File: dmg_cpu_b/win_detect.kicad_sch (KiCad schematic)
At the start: 127 parts

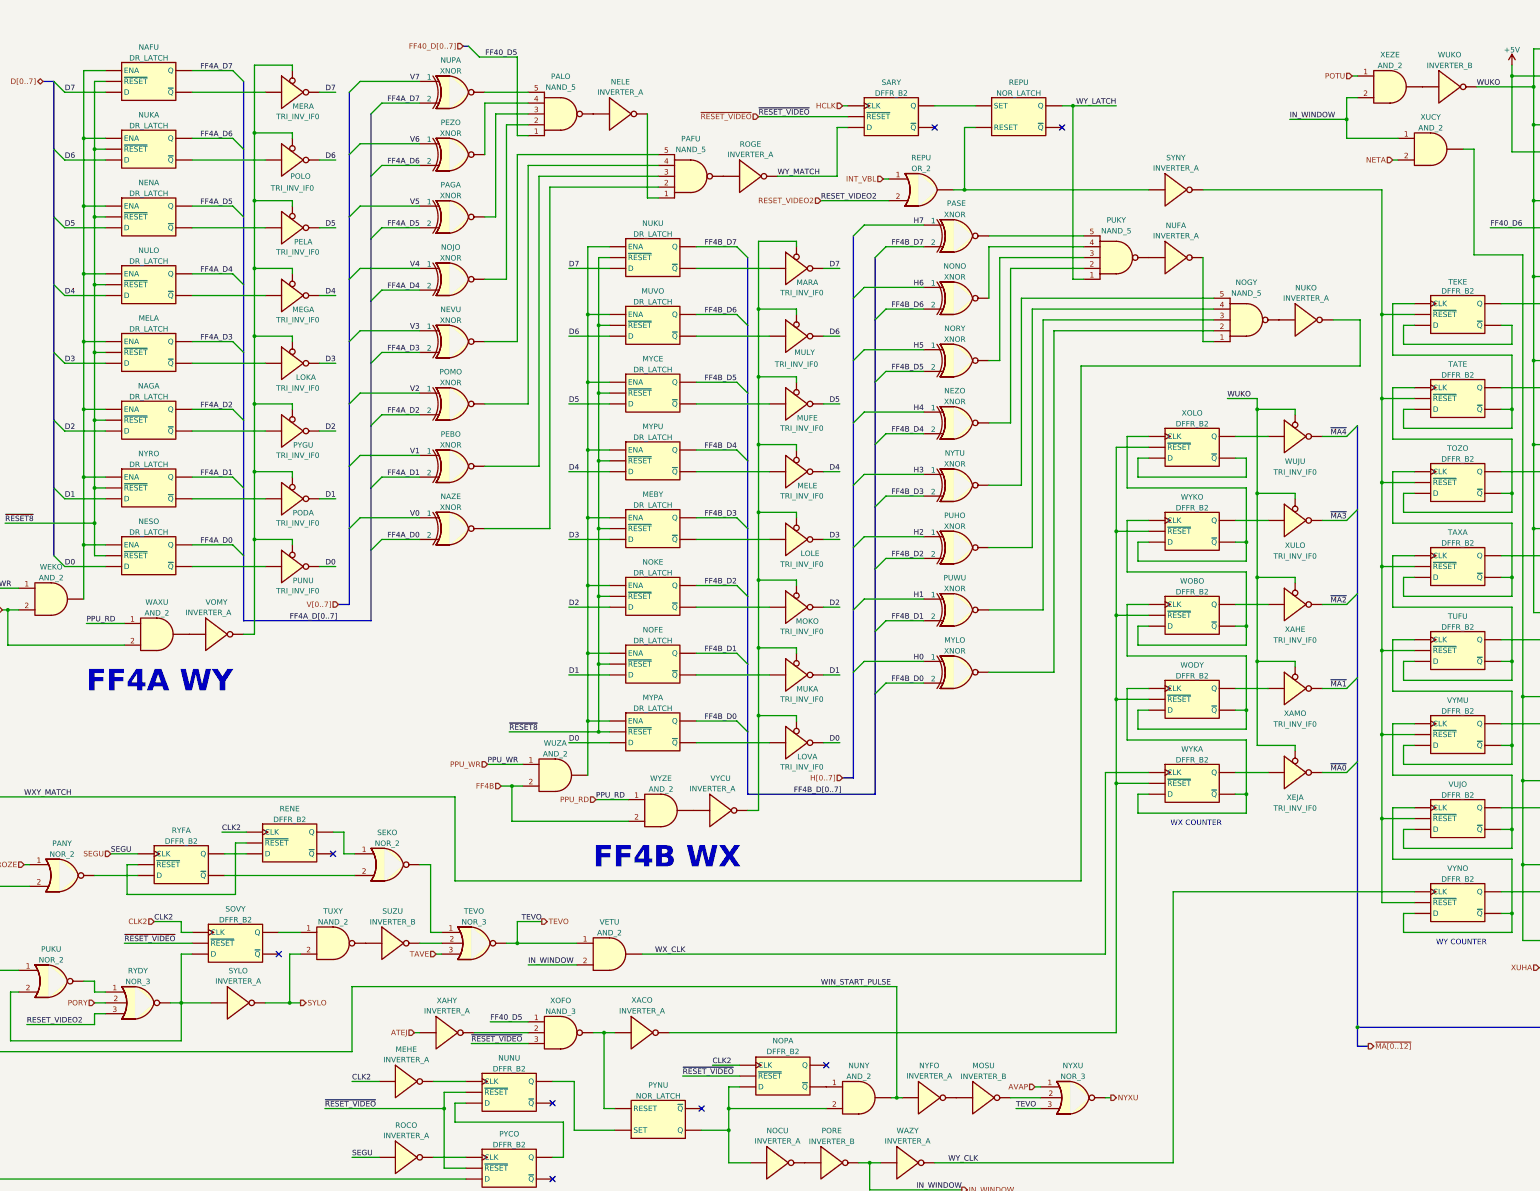
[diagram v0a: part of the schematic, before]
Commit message: Some mistakes found in APU sheets, notes added for clarity. Edit in PPU sheets following review.
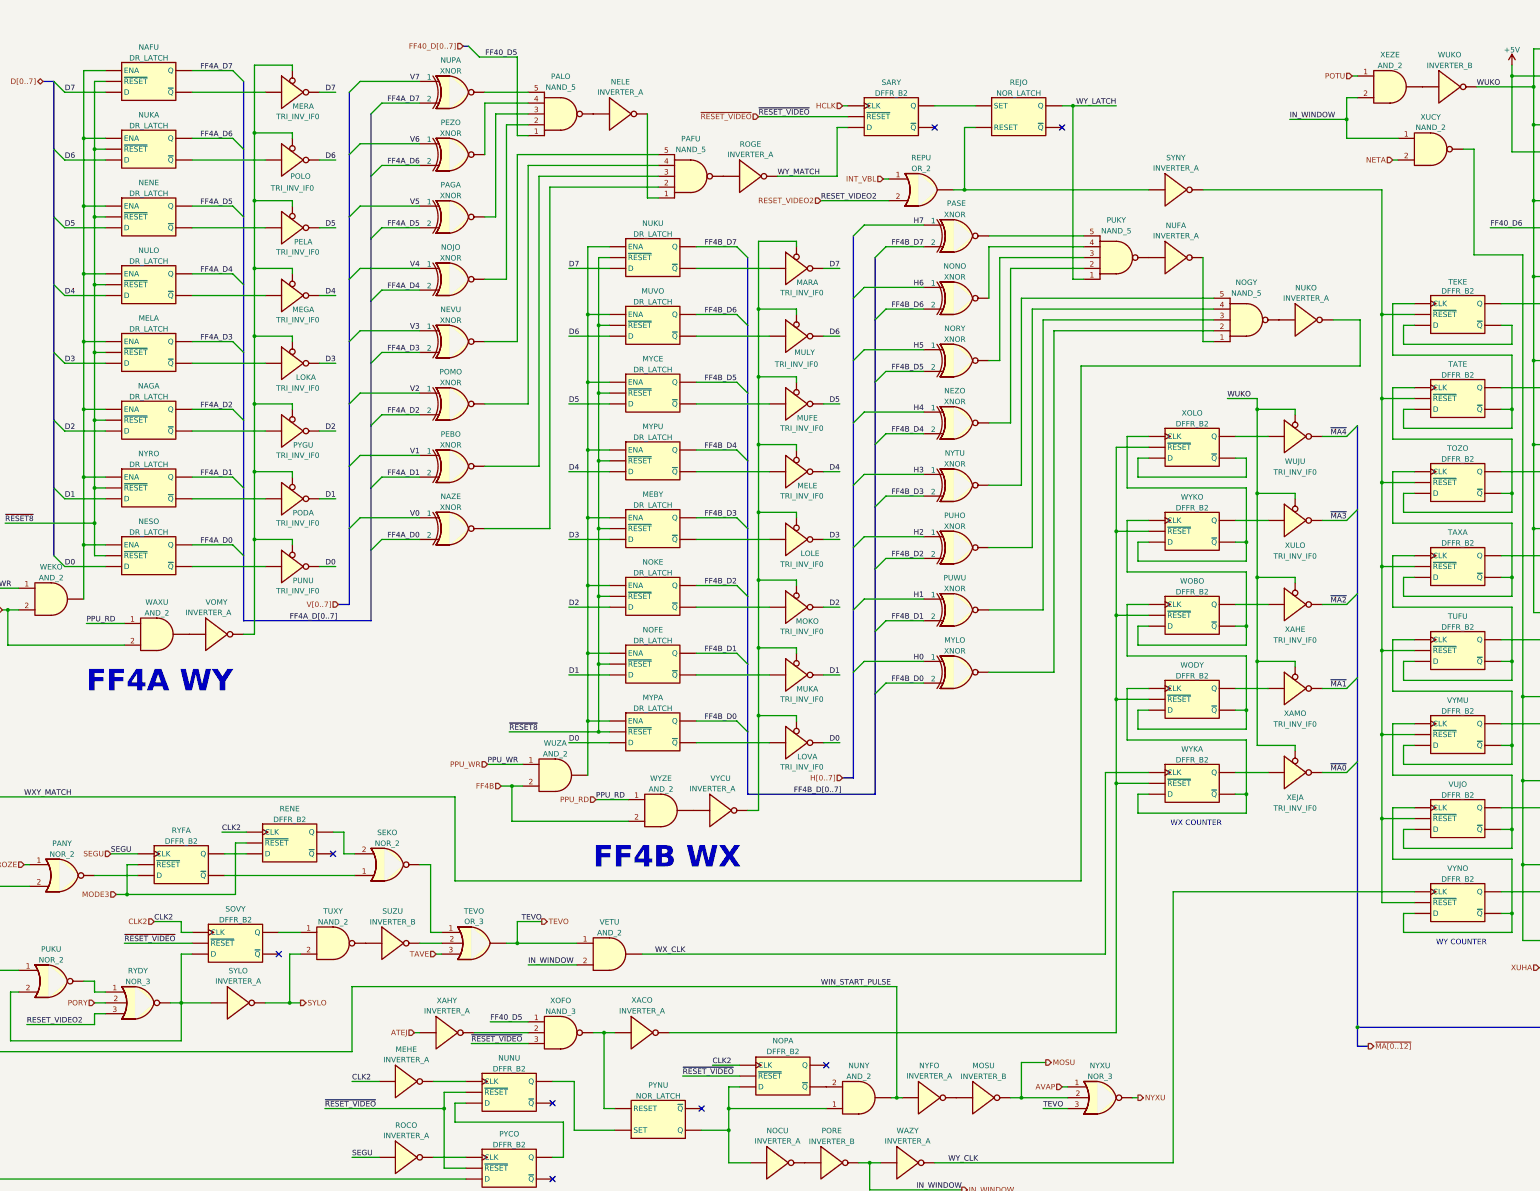
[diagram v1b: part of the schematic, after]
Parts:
- TEVO: value NOR_3 -> OR_3; symbol DMG_CPU_Cells:NOR_3 -> DMG_CPU_Cells:OR_3
- XUCY: value AND_2 -> NAND_2; symbol DMG_CPU_Cells:AND_2 -> DMG_CPU_Cells:NAND_2
- renumbered NENA to NENE, REPU to REJO
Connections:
- net at NOCU.1, NOPA.3 (D), PYNU.3 (Q): now also NUNY.1; no longer NUNY.2
- net at NOPA.5 (~{Q}): now also NUNY.2; no longer NUNY.1
- net MODE3: now reaches RENE.2 (~{RESET}), RENE.4 (~{RESET}), RYFA.2 (~{RESET}), RYFA.4 (~{RESET})
- net at RYFA.5 (~{Q}): now also SEKO.1; no longer SEKO.2
- net at RENE.6 (Q): now also SEKO.2; no longer SEKO.1
- net MOSU: now reaches MOSU.2, NYXU.2
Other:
- moved on the sheet: NYXU
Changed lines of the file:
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@@
   (junction (at 346.075 175.895) (diameter 0) (color 0 0 0 0)
   )
+  (junction (at 261.62 260.985) (diameter 0) (color 0 0 0 0)
+  )
   (junction (at 90.17 238.76) (diameter 0) (color 0 0 0 0)
   )
@@
   (junction (at 44.45 54.61) (diameter 0) (color 0 0 0 0)
   )
+  (junction (at 52.07 213.36) (diameter 0) (color 0 0 0 0)
+  )
   (junction (at 41.91 52.07) (diameter 0) (color 0 0 0 0)
   )
@@
     (stroke (width 0) (type default) (color 0 0 0 0))
   )
+  (wire (pts (xy 261.62 260.985) (xy 259.08 260.985))
+    (stroke (width 0) (type default) (color 0 0 0 0))
+  )
   (wire (pts (xy 104.775 274.955) (xy 111.125 274.955))
     (stroke (width 0) (type default) (color 0 0 0 0))
@@
     (stroke (width 0) (type default) (color 0 0 0 0))
   )
-  (wire (pts (xy 281.305 260.985) (xy 282.575 260.985))
+  (wire (pts (xy 287.655 260.985) (xy 288.925 260.985))
     (stroke (width 0) (type default) (color 0 0 0 0))
   )
@@
     (stroke (width 0) (type default) (color 0 0 0 0))
   )
+  (wire (pts (xy 261.62 252.73) (xy 267.335 252.73))
+    (stroke (width 0) (type default) (color 0 0 0 0))
+  )
   (wire (pts (xy 41.91 20.32) (xy 46.99 20.32))
     (stroke (width 0) (type default) (color 0 0 0 0))
@@
     (stroke (width 0) (type default) (color 0 0 0 0))
   )
+  (wire (pts (xy 49.53 213.36) (xy 52.07 213.36))
+    (stroke (width 0) (type default) (color 0 0 0 0))
+  )
   (bus (pts (xy 219.71 186.055) (xy 222.25 186.055))
     (stroke (width 0) (type default) (color 0 0 0 0))
@@
     (stroke (width 0) (type default) (color 0 0 0 0))
   )
-  (wire (pts (xy 266.065 263.525) (xy 260.35 263.525))
+  (wire (pts (xy 272.415 263.525) (xy 266.7 263.525))
     (stroke (width 0) (type default) (color 0 0 0 0))
   )
@@
     (stroke (width 0) (type default) (color 0 0 0 0))
   )
-  (wire (pts (xy 266.065 260.985) (xy 259.08 260.985))
+  (wire (pts (xy 272.415 260.985) (xy 261.62 260.985))
     (stroke (width 0) (type default) (color 0 0 0 0))
   )
@@
     (stroke (width 0) (type default) (color 0 0 0 0))
   )
+  (wire (pts (xy 261.62 260.985) (xy 261.62 252.73))
+    (stroke (width 0) (type default) (color 0 0 0 0))
+  )
   (wire (pts (xy 254 102.87) (xy 259.08 102.87))
     (stroke (width 0) (type default) (color 0 0 0 0))
@@
     (stroke (width 0) (type default) (color 0 0 0 0))
   )
-  (wire (pts (xy 264.795 258.445) (xy 266.065 258.445))
+  (wire (pts (xy 271.145 258.445) (xy 272.415 258.445))
     (stroke (width 0) (type default) (color 0 0 0 0))
   )
@@
     (effects (font (size 1.27 1.27)) (justify right bottom))
   )
-  (label "TEVO" (at 260.35 263.525 0)
+  (label "TEVO" (at 266.7 263.525 0)
     (effects (font (size 1.27 1.27)) (justify left bottom))
   )
@@
     (effects (font (size 1.27 1.27)) (justify right))
   )
-  (hierarchical_label "NYXU" (shape output) (at 282.575 260.985 0)
+  (hierarchical_label "NYXU" (shape output) (at 288.925 260.985 0)
     (effects (font (size 1.27 1.27)) (justify left))
   )
@@
     (effects (font (size 1.27 1.27)) (justify right))
   )
+  (hierarchical_label "MOSU" (shape output) (at 267.335 252.73 0)
+    (effects (font (size 1.27 1.27)) (justify left))
+  )
   (hierarchical_label "H[0..7]" (shape input) (at 219.71 186.055 180)
     (effects (font (size 1.27 1.27)) (justify right))
@@
     (effects (font (size 1.27 1.27)) (justify right))
   )
+  (hierarchical_label "MODE3" (shape input) (at 49.53 213.36 180)
+    (effects (font (size 1.27 1.27)) (justify right))
+  )
   (hierarchical_label "~{MA[0..12]}" (shape output) (at 342.9 248.92 0)
     (effects (font (size 1.27 1.27)) (justify left))
@@
     (effects (font (size 1.27 1.27)) (justify right))
   )
-  (hierarchical_label "AVAP" (shape input) (at 264.795 258.445 180)
+  (hierarchical_label "AVAP" (shape input) (at 271.145 258.445 180)
     (effects (font (size 1.27 1.27)) (justify right))
   )
@@
   (symbol (lib_id "DMG_CPU_Cells:NOR_LATCH") (at 260.985 31.115 0) (unit 1)
     (in_bom yes) (on_board yes) (fields_autoplaced)
-    (property "Reference" "REPU" (id 0) (at 260.985 23.0972 0))
+    (property "Reference" "REJO" (id 0) (at 260.985 23.0972 0))
     (property "Value" "NOR_LATCH" (id 1) (at 260.985 25.6341 0))
     (property "Footprint" "" (id 2) (at 260.985 31.115 0)
@@
     (pin "6")
   )
-  (symbol (lib_id "DMG_CPU_Cells:NOR_2") (at 113.03 206.375 0) (unit 1)
+  (symbol (lib_id "DMG_CPU_Cells:NOR_2") (at 113.03 206.375 0) (mirror x) (unit 1)
     (in_bom yes) (on_board yes) (fields_autoplaced)
     (property "Reference" "SEKO" (id 0) (at 113.0298 198.8652 0))
@@
       (effects (font (size 1.27 1.27)) hide)
     )
-    (property "Datasheet" "http://iceboy.a-singer.de/doc/dmg_cells.html#nor2" (id 3) (at 113.03 213.995 0)
+    (property "Datasheet" "http://iceboy.a-singer.de/doc/dmg_cells.html#nor2" (id 3) (at 113.03 198.755 0)
       (effects (font (size 1.27 1.27)) hide)
     )
@@
     (pin "1")
   )
-  (symbol (lib_id "DMG_CPU_Cells:AND_2") (at 223.52 260.985 0) (unit 1)
+  (symbol (lib_id "DMG_CPU_Cells:AND_2") (at 223.52 260.985 0) (mirror x) (unit 1)
     (in_bom yes) (on_board yes) (fields_autoplaced)
     (property "Reference" "NUNY" (id 0) (at 223.52 253.4752 0))
@@
       (effects (font (size 1.27 1.27)) hide)
     )
-    (property "Datasheet" "http://iceboy.a-singer.de/doc/dmg_cells.html#and2" (id 3) (at 223.52 268.605 0)
+    (property "Datasheet" "http://iceboy.a-singer.de/doc/dmg_cells.html#and2" (id 3) (at 223.52 253.365 0)
       (effects (font (size 1.27 1.27)) hide)
     )
@@
     (pin "6")
   )
-  (symbol (lib_id "DMG_CPU_Cells:NOR_3") (at 273.685 260.985 0) (unit 1)
+  (symbol (lib_id "DMG_CPU_Cells:NOR_3") (at 280.035 260.985 0) (unit 1)
     (in_bom yes) (on_board yes) (fields_autoplaced)
-    (property "Reference" "NYXU" (id 0) (at 273.6848 253.4752 0))
-    (property "Value" "NOR_3" (id 1) (at 273.6848 256.0121 0))
-    (property "Footprint" "" (id 2) (at 273.431 260.985 0)
+    (property "Reference" "NYXU" (id 0) (at 280.0348 253.4752 0))
+    (property "Value" "NOR_3" (id 1) (at 280.0348 256.0121 0))
+    (property "Footprint" "" (id 2) (at 279.781 260.985 0)
       (effects (font (size 1.27 1.27)) hide)
     )
-    (property "Datasheet" "http://iceboy.a-singer.de/doc/dmg_cells.html#nor3" (id 3) (at 273.685 268.605 0)
+    (property "Datasheet" "http://iceboy.a-singer.de/doc/dmg_cells.html#nor3" (id 3) (at 280.035 268.605 0)
       (effects (font (size 1.27 1.27)) hide)
     )
@@
     (pin "2")
   )
-  (symbol (lib_id "DMG_CPU_Cells:NOR_3") (at 133.35 224.79 0) (unit 1)
-    (in_bom yes) (on_board yes) (fields_autoplaced)
+  (symbol (lib_id "DMG_CPU_Cells:OR_3") (at 133.35 224.79 0) (unit 1)
+    (in_bom yes) (on_board yes)
     (property "Reference" "TEVO" (id 0) (at 133.3498 217.2802 0))
-    (property "Value" "NOR_3" (id 1) (at 133.3498 219.8171 0))
+    (property "Value" "OR_3" (id 1) (at 133.35 219.71 0))
     (property "Footprint" "" (id 2) (at 133.096 224.79 0)
       (effects (font (size 1.27 1.27)) hide)
     )
-    (property "Datasheet" "http://iceboy.a-singer.de/doc/dmg_cells.html#nor3" (id 3) (at 133.35 232.41 0)
+    (property "Datasheet" "http://iceboy.a-singer.de/doc/dmg_cells.html#or3" (id 3) (at 133.35 232.41 0)
       (effects (font (size 1.27 1.27)) hide)
     )
@@
     (pin "1")
   )
-  (symbol (lib_id "DMG_CPU_Cells:AND_2") (at 357.505 38.735 0) (unit 1)
-    (in_bom yes) (on_board yes) (fields_autoplaced)
+  (symbol (lib_id "DMG_CPU_Cells:NAND_2") (at 357.505 38.735 0) (unit 1)
+    (in_bom yes) (on_board yes)
     (property "Reference" "XUCY" (id 0) (at 357.505 31.2252 0))
-    (property "Value" "AND_2" (id 1) (at 357.505 33.7621 0))
+    (property "Value" "NAND_2" (id 1) (at 357.505 33.655 0))
     (property "Footprint" "" (id 2) (at 357.505 38.735 0)
       (effects (font (size 1.27 1.27)) hide)
     )
-    (property "Datasheet" "http://iceboy.a-singer.de/doc/dmg_cells.html#and2" (id 3) (at 357.505 46.355 0)
+    (property "Datasheet" "http://iceboy.a-singer.de/doc/dmg_cells.html#nand2" (id 3) (at 357.505 46.355 0)
       (effects (font (size 1.27 1.27)) hide)
     )
@@
   (symbol (lib_id "DMG_CPU_Cells:DR_LATCH") (at 57.15 54.61 0) (unit 1)
     (in_bom yes) (on_board yes) (fields_autoplaced)
-    (property "Reference" "NENA" (id 0) (at 57.15 46.5922 0))
+    (property "Reference" "NENE" (id 0) (at 57.15 46.5922 0))
     (property "Value" "DR_LATCH" (id 1) (at 57.15 49.1291 0))
     (property "Footprint" "" (id 2) (at 57.15 54.61 0)

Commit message: VRAM interface sheet added but various edits in existing sheets. Notable merge of RESET, CLOCKS and FF04 DIV sheets
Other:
- company: (none) -> CC-BY-SA-4.0 Régis Galland & Michael Singer -- Derived work from Furrtek
- title: (none) -> DMG CPU B
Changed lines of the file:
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@@
 (kicad_sch (version 20211123) (generator eeschema)
   (paper "A3")
+  (title_block
+    (title "DMG CPU B")
+    (date "2022-05-02")
+    (rev "0")
+    (company "CC-BY-SA-4.0 Régis Galland & Michael Singer -- Derived work from Furrtek")
+    (comment 1 "https://github.com/msinger/dmg-schematics")
+  )
   (junction (at 64.77 238.76) (diameter 0) (color 0 0 0 0)
   )

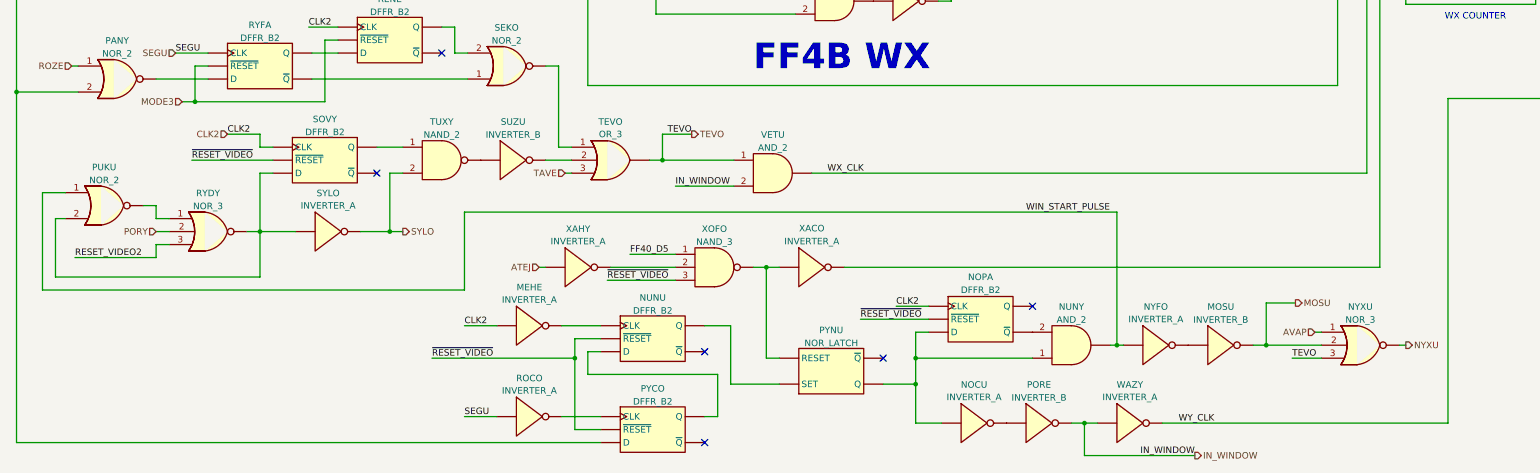
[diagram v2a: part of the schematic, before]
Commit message: more oam sheets added. Some are still work in progress.
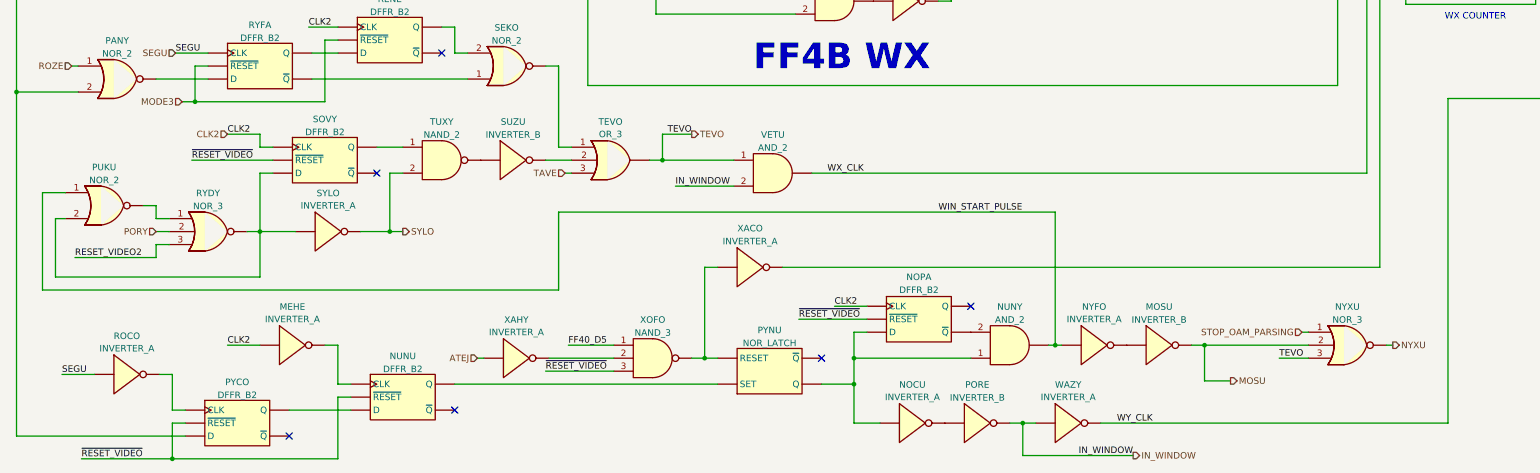
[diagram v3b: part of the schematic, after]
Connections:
- net AVAP renamed STOP_OAM_PARSING
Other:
- moved on the sheet: MEHE, MOSU, NOCU, NOPA, NUNU, NUNY, NYFO, NYXU, PORE, PYCO, PYNU, ROCO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
